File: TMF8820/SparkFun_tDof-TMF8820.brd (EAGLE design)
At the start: 25.4 x 25.4 mm, 54 parts, among them J4 QWIIC_RIGHT_ANGLE, J5 QWIIC_RIGHT_ANGLE

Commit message: Rotates "IO0" silk on bottom side of regular Qwiic versions of the product
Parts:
- U$19: device TMFTopSilk:#IO0#8 -> TMFBotSilk:#IO0#8
- turned U$19 to 270 degrees
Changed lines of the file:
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@@
 <layer number="45" name="Holes" color="7" fill="1" visible="yes" active="yes"/>
 <layer number="46" name="Milling" color="3" fill="1" visible="no" active="yes"/>
-<layer number="47" name="Measures" color="7" fill="1" visible="yes" active="yes"/>
+<layer number="47" name="Measures" color="7" fill="1" visible="no" active="yes"/>
 <layer number="48" name="Document" color="7" fill="1" visible="no" active="yes"/>
 <layer number="49" name="Reference" color="13" fill="1" visible="yes" active="yes"/>
@@
 <layer number="115" name="ReferenceISLANDS" color="7" fill="1" visible="no" active="no"/>
 <layer number="116" name="Patch_BOT" color="9" fill="4" visible="no" active="no"/>
-<layer number="117" name="PM_Ref" color="26" fill="1" visible="no" active="yes"/>
+<layer number="117" name="PM_Ref" color="26" fill="1" visible="yes" active="yes"/>
 <layer number="118" name="Rect_Pads" color="7" fill="1" visible="no" active="no"/>
-<layer number="119" name="PF_Ref" color="31" fill="1" visible="no" active="yes"/>
-<layer number="120" name="WFL_Ref" color="25" fill="1" visible="no" active="yes"/>
+<layer number="119" name="PF_Ref" color="31" fill="1" visible="yes" active="yes"/>
+<layer number="120" name="WFL_Ref" color="25" fill="1" visible="yes" active="yes"/>
 <layer number="121" name="_tsilk" color="7" fill="1" visible="no" active="no"/>
 <layer number="122" name="_bsilk" color="7" fill="1" visible="no" active="no"/>
@@
 <element name="U$12" library="TMFTopSilk" package="TMF88209" value="" x="12.7" y="17.78" smashed="yes"/>
 <element name="U$15" library="TMFBotSilk" package="#SYNC#8" value="" x="21.59" y="4.445" smashed="yes" rot="MR270"/>
-<element name="U$19" library="TMFTopSilk" package="#IO0#8" value="" x="19.05" y="3.683" smashed="yes" rot="MR90"/>
 <element name="U$24" library="TMFTopSilk" package="##INT##8" value="" x="16.51" y="3.683" smashed="yes" rot="MR270"/>
 <element name="U$26" library="TMFTopSilk" package="DTOF882188211" value="" x="12.7" y="19.685" smashed="yes" rot="MR0"/>
 <element name="U$27" library="TMFTopSilk" package="TMF88209" value="" x="12.7" y="17.78" smashed="yes" rot="MR0"/>
 <element name="U$13" library="SparkFun-Aesthetics" package="SFE_LOGO_NAME_FLAME_.1" value="" x="12.7" y="21.336" smashed="yes"/>
+<element name="U$19" library="TMFBotSilk" package="#IO0#8" value="" x="19.05" y="3.683" smashed="yes" rot="MR270"/>
 </elements>
 <signals>

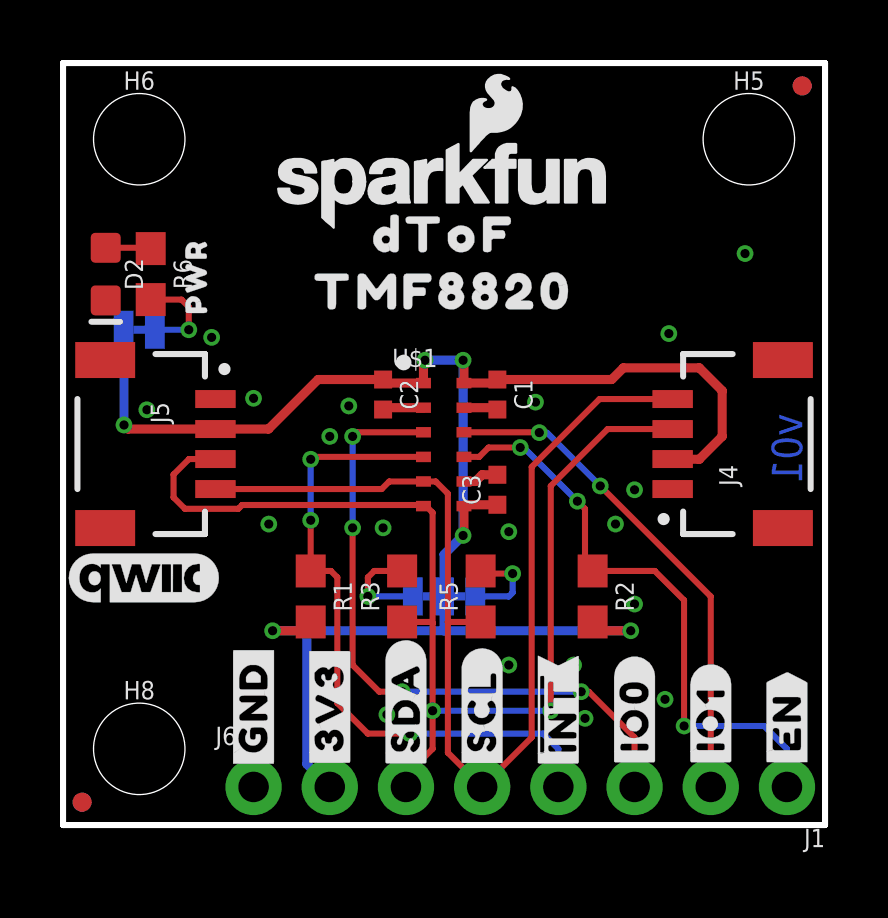
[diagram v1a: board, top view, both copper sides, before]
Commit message: Adds a two solder jumper for identifying whether the product has
the 8820 or 8821 - to the 8820 Qwiic Board
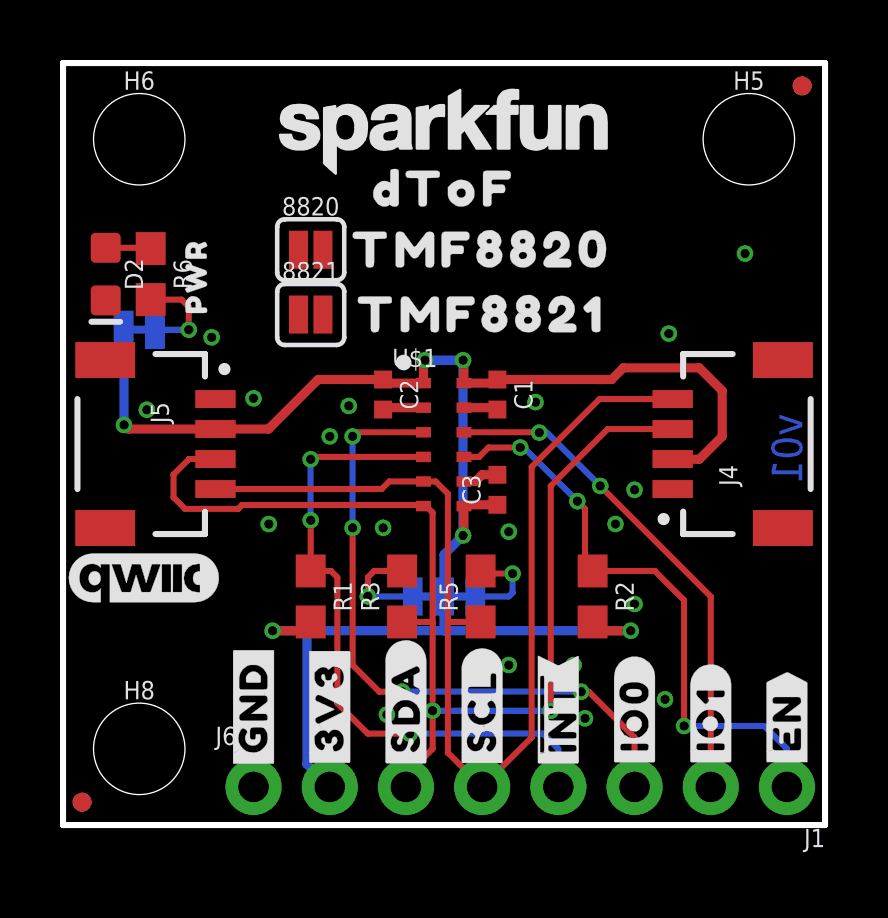
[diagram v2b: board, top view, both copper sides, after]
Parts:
- added 8820: JUMPER-SMT_2_NC_PASTE_SILK, SparkFun-Jumpers:SMT-JUMPER_2_NC_PASTE_SILK
- added 8821: JUMPER-SMT_2_NO_SILK, SparkFun-Jumpers:SMT-JUMPER_2_NO_SILK
- added U$25: (no value), TMFTopSilk:TMF882188210
- U$13: device SparkFun-Aesthetics:SFE_LOGO_NAME_FLAME_.1 -> SparkFun-Aesthetics:SFE_LOGO_NAME_.1
- U$27: device TMFTopSilk:TMF88209 -> TMFTopSilk:TMF882X882188211
- moved U$12 1.89 mm to (14.0, 19.2)
- moved U$13 1.78 mm to (12.7, 23.1)
- moved U$11 1.52 mm to (12.7, 21.2)
- moved U$27 0.25 mm to (12.7, 18.0)
- moved LOGO3 0.13 mm to (12.7, 21.3)
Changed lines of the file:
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@@
 <layer number="29" name="tStop" color="7" fill="3" visible="no" active="yes"/>
 <layer number="30" name="bStop" color="7" fill="6" visible="no" active="yes"/>
-<layer number="31" name="tCream" color="7" fill="4" visible="no" active="yes"/>
+<layer number="31" name="tCream" color="7" fill="4" visible="yes" active="yes"/>
 <layer number="32" name="bCream" color="7" fill="5" visible="no" active="yes"/>
 <layer number="33" name="tFinish" color="6" fill="3" visible="no" active="yes"/>
@@
 <attribute name="VALUE" value="2.2k" x="14.6812" y="7.62" size="0.6096" layer="27" font="vector" ratio="20" rot="R90" align="top-center"/>
 </element>
-<element name="LOGO3" library="SparkFun-Aesthetics" package="SFE_LOGO_NAME_FLAME_.1" value="SFE_LOGO_NAME_FLAME.1_INCH" x="12.827" y="21.336" smashed="yes" rot="MR0"/>
+<element name="LOGO3" library="SparkFun-Aesthetics" package="SFE_LOGO_NAME_FLAME_.1" value="SFE_LOGO_NAME_FLAME.1_INCH" x="12.7" y="21.336" smashed="yes" rot="MR0"/>
 <element name="U$6" library="SparkFun-Aesthetics" package="QWIIC_5MM" value="QWIIC_LOGO_5MM" x="2.667" y="8.255" smashed="yes"/>
 <element name="LOGO4" library="SparkFun-Aesthetics" package="OSHW-LOGO-S" value="OSHW-LOGOS" x="2.286" y="5.969" smashed="yes" rot="MR0"/>
@@
 <element name="U$9" library="TMFTopSilk" package="#IO1#8" value="" x="21.59" y="3.556" smashed="yes" rot="R90"/>
 <element name="U$10" library="TMFBotSilk" package="##INT##9" value="" x="16.51" y="3.683" smashed="yes" rot="R90"/>
-<element name="U$11" library="TMFTopSilk" package="DTOF882188211" value="" x="12.7" y="19.685" smashed="yes"/>
-<element name="U$12" library="TMFTopSilk" package="TMF88209" value="" x="12.7" y="17.78" smashed="yes"/>
+<element name="U$11" library="TMFTopSilk" package="DTOF882188211" value="" x="12.7" y="21.209" smashed="yes"/>
+<element name="U$12" library="TMFTopSilk" package="TMF88209" value="" x="13.97" y="19.177" smashed="yes"/>
 <element name="U$15" library="TMFBotSilk" package="#SYNC#8" value="" x="21.59" y="4.445" smashed="yes" rot="MR270"/>
 <element name="U$24" library="TMFTopSilk" package="##INT##8" value="" x="16.51" y="3.683" smashed="yes" rot="MR270"/>
 <element name="U$26" library="TMFTopSilk" package="DTOF882188211" value="" x="12.7" y="19.685" smashed="yes" rot="MR0"/>
-<element name="U$27" library="TMFTopSilk" package="TMF88209" value="" x="12.7" y="17.78" smashed="yes" rot="MR0"/>
-<element name="U$13" library="SparkFun-Aesthetics" package="SFE_LOGO_NAME_FLAME_.1" value="" x="12.7" y="21.336" smashed="yes"/>
 <element name="U$19" library="TMFBotSilk" package="#IO0#8" value="" x="19.05" y="3.683" smashed="yes" rot="MR270"/>
+<element name="8820" library="SparkFun-Jumpers" package="SMT-JUMPER_2_NC_PASTE_SILK" package3d_urn="urn:adsk.eagle:package:39282/1" value="JUMPER-SMT_2_NC_PASTE_SILK" x="8.255" y="19.177" smashed="yes">
+<attribute name="NAME" x="8.255" y="20.32" size="0.6096" layer="25" font="vector" ratio="20" align="bottom-center"/>
+<attribute name="VALUE" x="8.255" y="18.034" size="0.6096" layer="27" font="vector" ratio="20" align="top-center"/>
+</element>
+<element name="8821" library="SparkFun-Jumpers" package="SMT-JUMPER_2_NO_SILK" package3d_urn="urn:adsk.eagle:package:39279/1" value="JUMPER-SMT_2_NO_SILK" x="8.255" y="17.018" smashed="yes">
+<attribute name="NAME" x="8.255" y="18.161" size="0.6096" layer="25" font="vector" ratio="20" align="bottom-center"/>
+<attribute name="VALUE" x="8.255" y="15.875" size="0.6096" layer="27" font="vector" ratio="20" align="top-center"/>
+</element>
+<element name="U$13" library="SparkFun-Aesthetics" package="SFE_LOGO_NAME_.1" value="" x="12.7" y="23.114" smashed="yes"/>
+<element name="U$25" library="TMFTopSilk" package="TMF882188210" value="" x="13.97" y="17.018" smashed="yes"/>
+<element name="U$27" library="TMFTopSilk" package="TMF882X882188211" value="" x="12.7" y="18.034" smashed="yes" rot="MR0"/>
 </elements>
 <signals>

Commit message: Adds new product identifier pads to all designs, rolls 8820 version number to v10
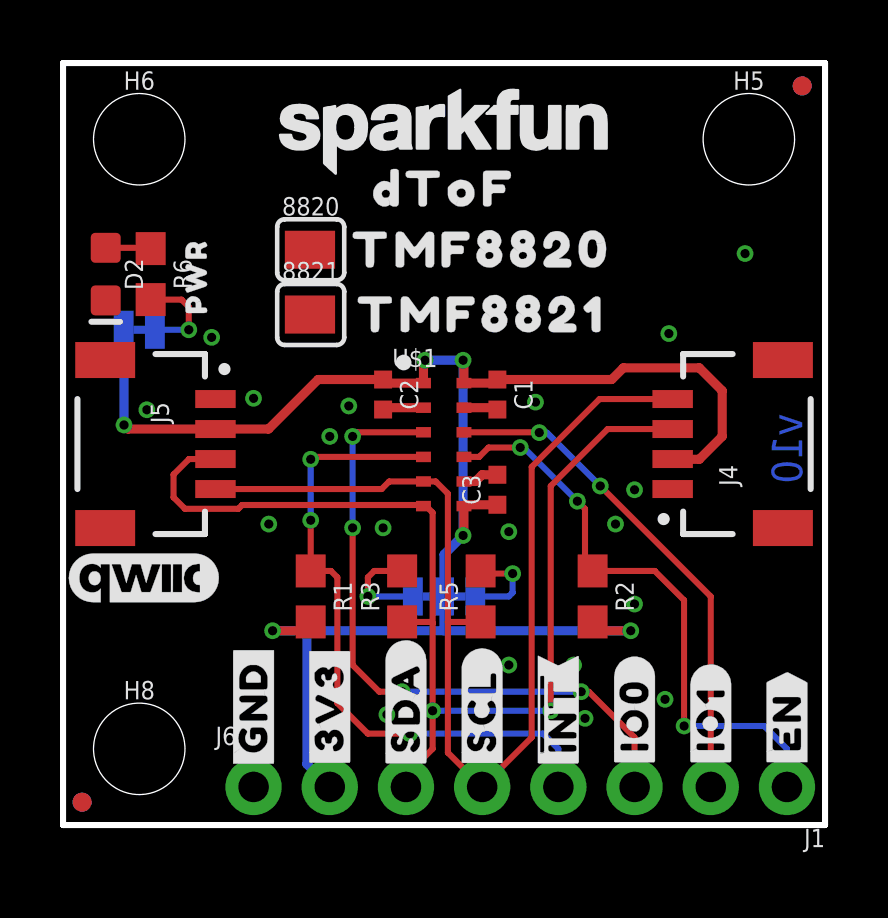
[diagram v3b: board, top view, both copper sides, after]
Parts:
- 8820: value JUMPER-SMT_2_NC_PASTE_SILK -> PROD_ID_PASTE_SILK; device SparkFun-Jumpers:SMT-JUMPER_2_NC_PASTE_SILK -> SparkFun-Aesthetics:PRODUCT_IDENT_PASTE_SILK
- 8821: value JUMPER-SMT_2_NO_SILK -> PROD_ID_NO-PASTE_SILK; device SparkFun-Jumpers:SMT-JUMPER_2_NO_SILK -> SparkFun-Aesthetics:PRODUCT_IDENT_NO_SILK
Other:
- board text added: "v10"
- board text removed: "v01"
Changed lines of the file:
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@@
 <wire x1="25.4" y1="25.4" x2="25.4" y2="0" width="0.2032" layer="20"/>
 <wire x1="25.4" y1="0" x2="0" y2="0" width="0.2032" layer="20"/>
-<text x="24.638" y="13.716" size="1.016" layer="16" font="vector" ratio="20" rot="SMR270">v01</text>
+<text x="24.638" y="13.716" size="1.016" layer="16" font="vector" ratio="20" rot="SMR270">v10</text>
 <text x="4.064" y="-5.588" size="1.778" layer="47" font="vector">Units in Inches</text>
 <dimension x1="0" y1="25.4" x2="25.4" y2="25.4" x3="12.7" y3="33.02" textsize="1.778" layer="47" unit="inch"/>
@@
 <element name="U$26" library="TMFTopSilk" package="DTOF882188211" value="" x="12.7" y="19.685" smashed="yes" rot="MR0"/>
 <element name="U$19" library="TMFBotSilk" package="#IO0#8" value="" x="19.05" y="3.683" smashed="yes" rot="MR270"/>
-<element name="8820" library="SparkFun-Jumpers" package="SMT-JUMPER_2_NC_PASTE_SILK" package3d_urn="urn:adsk.eagle:package:39282/1" value="JUMPER-SMT_2_NC_PASTE_SILK" x="8.255" y="19.177" smashed="yes">
+<element name="8820" library="SparkFun-Aesthetics" package="PRODUCT_IDENT_PASTE_SILK" value="PROD_ID_PASTE_SILK" x="8.255" y="19.177" smashed="yes">
 <attribute name="NAME" x="8.255" y="20.32" size="0.6096" layer="25" font="vector" ratio="20" align="bottom-center"/>
 <attribute name="VALUE" x="8.255" y="18.034" size="0.6096" layer="27" font="vector" ratio="20" align="top-center"/>
 </element>
-<element name="8821" library="SparkFun-Jumpers" package="SMT-JUMPER_2_NO_SILK" package3d_urn="urn:adsk.eagle:package:39279/1" value="JUMPER-SMT_2_NO_SILK" x="8.255" y="17.018" smashed="yes">
+<element name="8821" library="SparkFun-Aesthetics" package="PRODUCT_IDENT_NO_SILK" value="PROD_ID_NO-PASTE_SILK" x="8.255" y="17.018" smashed="yes">
 <attribute name="NAME" x="8.255" y="18.161" size="0.6096" layer="25" font="vector" ratio="20" align="bottom-center"/>
 <attribute name="VALUE" x="8.255" y="15.875" size="0.6096" layer="27" font="vector" ratio="20" align="top-center"/>

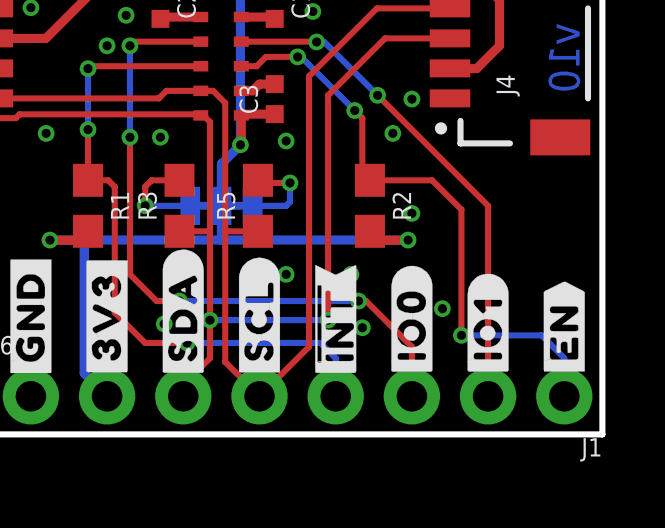
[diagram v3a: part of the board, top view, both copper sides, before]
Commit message: Changes all "IO" silk to be "GP" instead, increases Qwiic pill size on mini's
* Fixes orientation of I2C and LED silk on mini versions
* Increases SparkFun flame size on mini versions
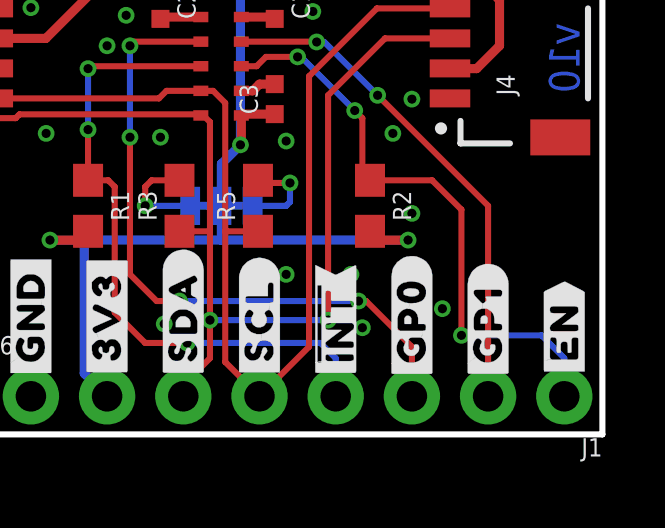
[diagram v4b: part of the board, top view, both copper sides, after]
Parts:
- U$19: device TMFBotSilk:#IO0#8 -> TMFBot:#GP0#8
- U$8: device TMFTopSilk:#IO0#8 -> TMFTop:#GP0#19
- U$9: device TMFTopSilk:#IO1#8 -> TMFTop:#GP1#8
- moved U$19 0.13 mm to (19.1, 3.81)
- moved U$8 0.13 mm to (19.1, 3.81)
- moved U$9 0.13 mm to (21.6, 3.68)
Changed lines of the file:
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@@
 <layer number="29" name="tStop" color="7" fill="3" visible="no" active="yes"/>
 <layer number="30" name="bStop" color="7" fill="6" visible="no" active="yes"/>
-<layer number="31" name="tCream" color="7" fill="4" visible="yes" active="yes"/>
+<layer number="31" name="tCream" color="7" fill="4" visible="no" active="yes"/>
 <layer number="32" name="bCream" color="7" fill="5" visible="no" active="yes"/>
 <layer number="33" name="tFinish" color="6" fill="3" visible="no" active="yes"/>
@@
 <element name="U$29" library="TMFBotSilk" package="ADDR#12" value="" x="12.319" y="11.684" smashed="yes" rot="MR0"/>
 <element name="U$30" library="TMFBotSilk" package="0X4113" value="" x="8.509" y="11.557" smashed="yes" rot="MR0"/>
-<element name="U$8" library="TMFTopSilk" package="#IO0#8" value="" x="19.05" y="3.683" smashed="yes" rot="R90"/>
-<element name="U$9" library="TMFTopSilk" package="#IO1#8" value="" x="21.59" y="3.556" smashed="yes" rot="R90"/>
 <element name="U$10" library="TMFBotSilk" package="##INT##9" value="" x="16.51" y="3.683" smashed="yes" rot="R90"/>
 <element name="U$11" library="TMFTopSilk" package="DTOF882188211" value="" x="12.7" y="21.209" smashed="yes"/>
@@
 <element name="U$24" library="TMFTopSilk" package="##INT##8" value="" x="16.51" y="3.683" smashed="yes" rot="MR270"/>
 <element name="U$26" library="TMFTopSilk" package="DTOF882188211" value="" x="12.7" y="19.685" smashed="yes" rot="MR0"/>
-<element name="U$19" library="TMFBotSilk" package="#IO0#8" value="" x="19.05" y="3.683" smashed="yes" rot="MR270"/>
 <element name="8820" library="SparkFun-Aesthetics" package="PRODUCT_IDENT_PASTE_SILK" value="PROD_ID_PASTE_SILK" x="8.255" y="19.177" smashed="yes">
 <attribute name="NAME" x="8.255" y="20.32" size="0.6096" layer="25" font="vector" ratio="20" align="bottom-center"/>
@@
 <element name="U$25" library="TMFTopSilk" package="TMF882188210" value="" x="13.97" y="17.018" smashed="yes"/>
 <element name="U$27" library="TMFTopSilk" package="TMF882X882188211" value="" x="12.7" y="18.034" smashed="yes" rot="MR0"/>
+<element name="U$8" library="TMFTop" package="#GP0#19" value="" x="19.05" y="3.81" smashed="yes" rot="R90"/>
+<element name="U$9" library="TMFTop" package="#GP1#8" value="" x="21.59" y="3.683" smashed="yes" rot="R90"/>
+<element name="U$19" library="TMFBot" package="#GP0#8" value="" x="19.05" y="3.81" smashed="yes" rot="MR270"/>
 </elements>
 <signals>

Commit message: Fixes Sync silk on GP1 through hole on Qwiic sized designs
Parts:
- U$19: device TMFBot:#GP0#8 -> TMFBot:#GP1#8
- moved U$19 2.54 mm to (21.6, 3.68)
- moved U$15 2.54 mm to (19.1, 4.45)
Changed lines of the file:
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@@
 <element name="U$11" library="TMFTopSilk" package="DTOF882188211" value="" x="12.7" y="21.209" smashed="yes"/>
 <element name="U$12" library="TMFTopSilk" package="TMF88209" value="" x="13.97" y="19.177" smashed="yes"/>
-<element name="U$15" library="TMFBotSilk" package="#SYNC#8" value="" x="21.59" y="4.445" smashed="yes" rot="MR270"/>
+<element name="U$15" library="TMFBotSilk" package="#SYNC#8" value="" x="19.05" y="4.445" smashed="yes" rot="MR270"/>
 <element name="U$24" library="TMFTopSilk" package="##INT##8" value="" x="16.51" y="3.683" smashed="yes" rot="MR270"/>
 <element name="U$26" library="TMFTopSilk" package="DTOF882188211" value="" x="12.7" y="19.685" smashed="yes" rot="MR0"/>
@@
 <element name="U$8" library="TMFTop" package="#GP0#19" value="" x="19.05" y="3.81" smashed="yes" rot="R90"/>
 <element name="U$9" library="TMFTop" package="#GP1#8" value="" x="21.59" y="3.683" smashed="yes" rot="R90"/>
-<element name="U$19" library="TMFBot" package="#GP0#8" value="" x="19.05" y="3.81" smashed="yes" rot="MR270"/>
+<element name="U$19" library="TMFBot" package="#GP1#8" value="" x="21.59" y="3.683" smashed="yes" rot="MR270"/>
 </elements>
 <signals>
